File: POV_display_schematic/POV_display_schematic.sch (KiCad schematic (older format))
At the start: 124 parts, among them J1 5-Wire Programming Port, J2 BOOT SELECT, Q1 MMBT3904, Q2 MMBT3906, U1 74HC595, U10 74HC595, U11 HT7325, U2 74HC595, U3 74HC595, U4 74HC595, U5 74HC595, U6 LN4913, U7 74HC595, U8 74HC595, U9 STM32L051C8Tx, Y1 32.768 KHz

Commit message: Uploaded offline work
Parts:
- removed C6: 1uF, Capacitor_SMD:C_1206_3216Metric_Pad1.33x1.80mm_HandSolder, symbol Device:C
- removed J1: 5-Wire Programming Port, Connector_PinHeader_2.54mm:PinHeader_1x05_P2.54mm_Vertical, symbol Connector:Conn_01x05_Female
- removed J2: BOOT SELECT, Connector_PinHeader_2.54mm:PinHeader_1x02_P2.54mm_Vertical, symbol Connector:Conn_01x02_Male
- removed R65: 10K, Resistor_SMD:R_0603_1608Metric_Pad0.98x0.95mm_HandSolder, symbol Device:R
- removed U6: LN4913, Package_TO_SOT_SMD:TSOT-23_HandSoldering, symbol POV_display_schematic:LN4913
- added C2, C4: 10uF, Capacitor_SMD:C_0805_2012Metric_Pad1.18x1.45mm_HandSolder, symbol Device:C
- added D1: Green, LED_SMD:LED_0805_2012Metric_Pad1.15x1.40mm_HandSolder, symbol Device:LED
- added D2: Red, LED_SMD:LED_0805_2012Metric_Pad1.15x1.40mm_HandSolder, symbol Device:LED
- added D24: D_Photo, LED_THT:LED_D5.0mm, symbol Device:D_Photo
- added H1, H2, H3, H4: M3, MountingHole:MountingHole_3.2mm_M3, symbol Mechanical:MountingHole
- added J1: USB_B_Micro, Connector_USB:USB_Micro-B_Molex-105017-0001, symbol Connector:USB_B_Micro
- added J3: HC05/06 Port, Connector_PinHeader_2.54mm:PinHeader_1x04_P2.54mm_Vertical, symbol Connector:Conn_01x04_Female
- added J4: 6PinDebugPort, Connector_IDC:IDC-Header_2x03_P2.54mm_Vertical, symbol MYCLEO:6PinDebugPort
- added R1, R2: 1K, Resistor_SMD:R_0805_2012Metric_Pad1.20x1.40mm_HandSolder, symbol Device:R
- added R10: 10K, Resistor_SMD:R_0805_2012Metric_Pad1.20x1.40mm_HandSolder, symbol Device:R
- added R3, R4: 47K, Resistor_SMD:R_0805_2012Metric_Pad1.20x1.40mm_HandSolder, symbol Device:R
- added R5: 4K7, Resistor_SMD:R_0805_2012Metric_Pad1.20x1.40mm_HandSolder, symbol Device:R
- added SW1: RST, custom_buttons_switches:TSB008, symbol Switch:SW_Push
- added SW2: BOOT, custom_buttons_switches:TSB008, symbol Switch:SW_Push
- added TP1, TP2, TP3, TP4, TP5, TP6: TestPoint, TestPoint:TestPoint_Pad_2.0x2.0mm, symbol Connector:TestPoint
- added U2: TP4056, Package_SO:SOP-8_3.9x4.9mm_P1.27mm, symbol Battery_Management_Custom:TP4056
- C1: renamed from C15; footprint Capacitor_SMD:C_1206_3216Metric_Pad1.33x1.80mm_HandSolder -> Capacitor_SMD:C_0805_2012Metric_Pad1.18x1.45mm_HandSolder
- C10: renamed from C9; footprint Capacitor_SMD:C_1206_3216Metric_Pad1.33x1.80mm_HandSolder -> Capacitor_SMD:C_0805_2012Metric_Pad1.18x1.45mm_HandSolder
- C11: renamed from C5; footprint Capacitor_SMD:C_1206_3216Metric_Pad1.33x1.80mm_HandSolder -> Capacitor_SMD:C_0805_2012Metric_Pad1.18x1.45mm_HandSolder
- C12: renamed from C11; footprint Capacitor_SMD:C_1206_3216Metric_Pad1.33x1.80mm_HandSolder -> Capacitor_SMD:C_0805_2012Metric_Pad1.18x1.45mm_HandSolder
- C13: renamed from C7; footprint Capacitor_SMD:C_1206_3216Metric_Pad1.33x1.80mm_HandSolder -> Capacitor_SMD:C_0805_2012Metric_Pad1.18x1.45mm_HandSolder
- C14: renamed from C10; footprint Capacitor_SMD:C_1206_3216Metric_Pad1.33x1.80mm_HandSolder -> Capacitor_SMD:C_0805_2012Metric_Pad1.18x1.45mm_HandSolder
- C15: renamed from C17; footprint Capacitor_SMD:C_1206_3216Metric_Pad1.33x1.80mm_HandSolder -> Capacitor_SMD:C_0805_2012Metric_Pad1.18x1.45mm_HandSolder
- C16: renamed from C14; footprint Capacitor_SMD:C_1206_3216Metric_Pad1.33x1.80mm_HandSolder -> Capacitor_SMD:C_0805_2012Metric_Pad1.18x1.45mm_HandSolder
- C3: renamed from C16; footprint Capacitor_SMD:C_1206_3216Metric_Pad1.33x1.80mm_HandSolder -> Capacitor_SMD:C_0805_2012Metric_Pad1.18x1.45mm_HandSolder
- C5: renamed from C1; footprint Capacitor_SMD:C_1206_3216Metric_Pad1.33x1.80mm_HandSolder -> Capacitor_SMD:C_0805_2012Metric_Pad1.18x1.45mm_HandSolder
- C6: renamed from C2; footprint Capacitor_SMD:C_1206_3216Metric_Pad1.33x1.80mm_HandSolder -> Capacitor_SMD:C_0805_2012Metric_Pad1.18x1.45mm_HandSolder
- C7: renamed from C3; footprint Capacitor_SMD:C_1206_3216Metric_Pad1.33x1.80mm_HandSolder -> Capacitor_SMD:C_0805_2012Metric_Pad1.18x1.45mm_HandSolder
- C8: footprint Capacitor_SMD:C_1206_3216Metric_Pad1.33x1.80mm_HandSolder -> Capacitor_SMD:C_0805_2012Metric_Pad1.18x1.45mm_HandSolder
- C9: renamed from C4; footprint Capacitor_SMD:C_1206_3216Metric_Pad1.33x1.80mm_HandSolder -> Capacitor_SMD:C_0805_2012Metric_Pad1.18x1.45mm_HandSolder
- R11: renamed from R69; footprint Resistor_SMD:R_1206_3216Metric_Pad1.30x1.75mm_HandSolder -> Resistor_SMD:R_0805_2012Metric_Pad1.20x1.40mm_HandSolder
- R12: renamed from R1; footprint Resistor_SMD:R_0603_1608Metric_Pad0.98x0.95mm_HandSolder -> Resistor_SMD:R_0603_1608Metric
- R13: renamed from R2; footprint Resistor_SMD:R_0603_1608Metric_Pad0.98x0.95mm_HandSolder -> Resistor_SMD:R_0603_1608Metric
- R14: renamed from R3; footprint Resistor_SMD:R_0603_1608Metric_Pad0.98x0.95mm_HandSolder -> Resistor_SMD:R_0603_1608Metric
- R15: renamed from R4; footprint Resistor_SMD:R_0603_1608Metric_Pad0.98x0.95mm_HandSolder -> Resistor_SMD:R_0603_1608Metric
- R16: renamed from R5; footprint Resistor_SMD:R_0603_1608Metric_Pad0.98x0.95mm_HandSolder -> Resistor_SMD:R_0603_1608Metric
- R17: renamed from R6; footprint Resistor_SMD:R_0603_1608Metric_Pad0.98x0.95mm_HandSolder -> Resistor_SMD:R_0603_1608Metric
- R18: renamed from R7; footprint Resistor_SMD:R_0603_1608Metric_Pad0.98x0.95mm_HandSolder -> Resistor_SMD:R_0603_1608Metric
- R19: renamed from R8; footprint Resistor_SMD:R_0603_1608Metric_Pad0.98x0.95mm_HandSolder -> Resistor_SMD:R_0603_1608Metric
- R20: renamed from R9; footprint Resistor_SMD:R_0603_1608Metric_Pad0.98x0.95mm_HandSolder -> Resistor_SMD:R_0603_1608Metric
- R21: renamed from R10; footprint Resistor_SMD:R_0603_1608Metric_Pad0.98x0.95mm_HandSolder -> Resistor_SMD:R_0603_1608Metric
- R22: renamed from R11; footprint Resistor_SMD:R_0603_1608Metric_Pad0.98x0.95mm_HandSolder -> Resistor_SMD:R_0603_1608Metric
- R23: renamed from R12; footprint Resistor_SMD:R_0603_1608Metric_Pad0.98x0.95mm_HandSolder -> Resistor_SMD:R_0603_1608Metric
- R24: renamed from R13; footprint Resistor_SMD:R_0603_1608Metric_Pad0.98x0.95mm_HandSolder -> Resistor_SMD:R_0603_1608Metric
- R25: renamed from R14; footprint Resistor_SMD:R_0603_1608Metric_Pad0.98x0.95mm_HandSolder -> Resistor_SMD:R_0603_1608Metric
- R26: renamed from R15; footprint Resistor_SMD:R_0603_1608Metric_Pad0.98x0.95mm_HandSolder -> Resistor_SMD:R_0603_1608Metric
- R27: renamed from R16; footprint Resistor_SMD:R_0603_1608Metric_Pad0.98x0.95mm_HandSolder -> Resistor_SMD:R_0603_1608Metric
- R28: renamed from R17; footprint Resistor_SMD:R_0603_1608Metric_Pad0.98x0.95mm_HandSolder -> Resistor_SMD:R_0603_1608Metric
- R29: renamed from R18; footprint Resistor_SMD:R_0603_1608Metric_Pad0.98x0.95mm_HandSolder -> Resistor_SMD:R_0603_1608Metric
- R30: renamed from R19; footprint Resistor_SMD:R_0603_1608Metric_Pad0.98x0.95mm_HandSolder -> Resistor_SMD:R_0603_1608Metric
- R31: renamed from R20; footprint Resistor_SMD:R_0603_1608Metric_Pad0.98x0.95mm_HandSolder -> Resistor_SMD:R_0603_1608Metric
- R32: renamed from R21; footprint Resistor_SMD:R_0603_1608Metric_Pad0.98x0.95mm_HandSolder -> Resistor_SMD:R_0603_1608Metric
- R33: renamed from R22; footprint Resistor_SMD:R_0603_1608Metric_Pad0.98x0.95mm_HandSolder -> Resistor_SMD:R_0603_1608Metric
- R34: renamed from R23; footprint Resistor_SMD:R_0603_1608Metric_Pad0.98x0.95mm_HandSolder -> Resistor_SMD:R_0603_1608Metric
- R35: renamed from R24; footprint Resistor_SMD:R_0603_1608Metric_Pad0.98x0.95mm_HandSolder -> Resistor_SMD:R_0603_1608Metric
- R36: renamed from R25; footprint Resistor_SMD:R_0603_1608Metric_Pad0.98x0.95mm_HandSolder -> Resistor_SMD:R_0603_1608Metric
- R37: renamed from R26; footprint Resistor_SMD:R_0603_1608Metric_Pad0.98x0.95mm_HandSolder -> Resistor_SMD:R_0603_1608Metric
- R38: renamed from R27; footprint Resistor_SMD:R_0603_1608Metric_Pad0.98x0.95mm_HandSolder -> Resistor_SMD:R_0603_1608Metric
- R39: renamed from R28; footprint Resistor_SMD:R_0603_1608Metric_Pad0.98x0.95mm_HandSolder -> Resistor_SMD:R_0603_1608Metric
- R40: renamed from R29; footprint Resistor_SMD:R_0603_1608Metric_Pad0.98x0.95mm_HandSolder -> Resistor_SMD:R_0603_1608Metric
- R41: renamed from R30; footprint Resistor_SMD:R_0603_1608Metric_Pad0.98x0.95mm_HandSolder -> Resistor_SMD:R_0603_1608Metric
- R42: renamed from R31; footprint Resistor_SMD:R_0603_1608Metric_Pad0.98x0.95mm_HandSolder -> Resistor_SMD:R_0603_1608Metric
- R43: renamed from R32; footprint Resistor_SMD:R_0603_1608Metric_Pad0.98x0.95mm_HandSolder -> Resistor_SMD:R_0603_1608Metric
- R44: renamed from R33; footprint Resistor_SMD:R_0603_1608Metric_Pad0.98x0.95mm_HandSolder -> Resistor_SMD:R_0603_1608Metric
- R45: renamed from R34; footprint Resistor_SMD:R_0603_1608Metric_Pad0.98x0.95mm_HandSolder -> Resistor_SMD:R_0603_1608Metric
- R46: renamed from R35; footprint Resistor_SMD:R_0603_1608Metric_Pad0.98x0.95mm_HandSolder -> Resistor_SMD:R_0603_1608Metric
- R47: renamed from R36; footprint Resistor_SMD:R_0603_1608Metric_Pad0.98x0.95mm_HandSolder -> Resistor_SMD:R_0603_1608Metric
- R48: renamed from R37; footprint Resistor_SMD:R_0603_1608Metric_Pad0.98x0.95mm_HandSolder -> Resistor_SMD:R_0603_1608Metric
- R49: renamed from R38; footprint Resistor_SMD:R_0603_1608Metric_Pad0.98x0.95mm_HandSolder -> Resistor_SMD:R_0603_1608Metric
- R50: renamed from R39; footprint Resistor_SMD:R_0603_1608Metric_Pad0.98x0.95mm_HandSolder -> Resistor_SMD:R_0603_1608Metric
- R51: renamed from R40; footprint Resistor_SMD:R_0603_1608Metric_Pad0.98x0.95mm_HandSolder -> Resistor_SMD:R_0603_1608Metric
- R52: renamed from R41; footprint Resistor_SMD:R_0603_1608Metric_Pad0.98x0.95mm_HandSolder -> Resistor_SMD:R_0603_1608Metric
- R53: renamed from R42; footprint Resistor_SMD:R_0603_1608Metric_Pad0.98x0.95mm_HandSolder -> Resistor_SMD:R_0603_1608Metric
- R54: renamed from R43; footprint Resistor_SMD:R_0603_1608Metric_Pad0.98x0.95mm_HandSolder -> Resistor_SMD:R_0603_1608Metric
- R55: renamed from R44; footprint Resistor_SMD:R_0603_1608Metric_Pad0.98x0.95mm_HandSolder -> Resistor_SMD:R_0603_1608Metric
- R56: renamed from R45; footprint Resistor_SMD:R_0603_1608Metric_Pad0.98x0.95mm_HandSolder -> Resistor_SMD:R_0603_1608Metric
- R57: renamed from R46; footprint Resistor_SMD:R_0603_1608Metric_Pad0.98x0.95mm_HandSolder -> Resistor_SMD:R_0603_1608Metric
- R58: renamed from R47; footprint Resistor_SMD:R_0603_1608Metric_Pad0.98x0.95mm_HandSolder -> Resistor_SMD:R_0603_1608Metric
- R59: renamed from R48; footprint Resistor_SMD:R_0603_1608Metric_Pad0.98x0.95mm_HandSolder -> Resistor_SMD:R_0603_1608Metric
- R6: renamed from R66; footprint Resistor_SMD:R_1206_3216Metric_Pad1.30x1.75mm_HandSolder -> Resistor_SMD:R_0805_2012Metric_Pad1.20x1.40mm_HandSolder
- R60: renamed from R49; footprint Resistor_SMD:R_0603_1608Metric_Pad0.98x0.95mm_HandSolder -> Resistor_SMD:R_0603_1608Metric
- R61: renamed from R50; footprint Resistor_SMD:R_0603_1608Metric_Pad0.98x0.95mm_HandSolder -> Resistor_SMD:R_0603_1608Metric
- R62: renamed from R51; footprint Resistor_SMD:R_0603_1608Metric_Pad0.98x0.95mm_HandSolder -> Resistor_SMD:R_0603_1608Metric
- R63: renamed from R52; footprint Resistor_SMD:R_0603_1608Metric_Pad0.98x0.95mm_HandSolder -> Resistor_SMD:R_0603_1608Metric
- R64: renamed from R53; footprint Resistor_SMD:R_0603_1608Metric_Pad0.98x0.95mm_HandSolder -> Resistor_SMD:R_0603_1608Metric
- R65: renamed from R54; footprint Resistor_SMD:R_0603_1608Metric_Pad0.98x0.95mm_HandSolder -> Resistor_SMD:R_0603_1608Metric
- R66: renamed from R55; footprint Resistor_SMD:R_0603_1608Metric_Pad0.98x0.95mm_HandSolder -> Resistor_SMD:R_0603_1608Metric
- R67: renamed from R56; footprint Resistor_SMD:R_0603_1608Metric_Pad0.98x0.95mm_HandSolder -> Resistor_SMD:R_0603_1608Metric
- R68: renamed from R57; footprint Resistor_SMD:R_0603_1608Metric_Pad0.98x0.95mm_HandSolder -> Resistor_SMD:R_0603_1608Metric
- R69: renamed from R58; footprint Resistor_SMD:R_0603_1608Metric_Pad0.98x0.95mm_HandSolder -> Resistor_SMD:R_0603_1608Metric
- R7: renamed from R64; footprint Resistor_SMD:R_0603_1608Metric_Pad0.98x0.95mm_HandSolder -> Resistor_SMD:R_0805_2012Metric_Pad1.20x1.40mm_HandSolder
- R70: renamed from R59; footprint Resistor_SMD:R_0603_1608Metric_Pad0.98x0.95mm_HandSolder -> Resistor_SMD:R_0603_1608Metric
- R71: renamed from R60; footprint Resistor_SMD:R_0603_1608Metric_Pad0.98x0.95mm_HandSolder -> Resistor_SMD:R_0603_1608Metric
- R72: renamed from R61; footprint Resistor_SMD:R_0603_1608Metric_Pad0.98x0.95mm_HandSolder -> Resistor_SMD:R_0603_1608Metric
- R73: renamed from R62; footprint Resistor_SMD:R_0603_1608Metric_Pad0.98x0.95mm_HandSolder -> Resistor_SMD:R_0603_1608Metric
- R74: renamed from R63; footprint Resistor_SMD:R_0603_1608Metric_Pad0.98x0.95mm_HandSolder -> Resistor_SMD:R_0603_1608Metric
- R8: renamed from R67; footprint Resistor_SMD:R_1206_3216Metric_Pad1.30x1.75mm_HandSolder -> Resistor_SMD:R_0805_2012Metric_Pad1.20x1.40mm_HandSolder
- R9: renamed from R68; footprint Resistor_SMD:R_1206_3216Metric_Pad1.30x1.75mm_HandSolder -> Resistor_SMD:R_0805_2012Metric_Pad1.20x1.40mm_HandSolder
- renumbered C12 to C17, C13 to C18, D8 to D10, D9 to D11, D10 to D12, D11 to D13, D12 to D14, D13 to D15, D14 to D16, D15 to D17, D16 to D18, D17 to D19, D18 to D20, D19 to D21, D20 to D22, D21 to D23, D1 to D3, D2 to D4, D3 to D5, D4 to D6, D5 to D7, D6 to D8, D7 to D9, Q1 to Q2, Q2 to Q3, U11 to U1, U4 to U10, U10 to U11, U5 to U3, U1 to U4, U2 to U5, U7 to U6, U3 to U7
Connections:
- net +BATT: now also C4.1, TP6.1, U2.5 (Bat)
- net BAT_EN: now also U9.12 (PA2); no longer U9.46 (PB9)
- net BAT_IN: now also U9.13 (PA3), TP4.1; no longer U9.10 (PA0)
- net GND: now also C2.2, C4.2, D24.2 (A), J1.4 (ID), J1.5 (GND), J1.6 (Shield), J3.2 (Pin_2), J4.1 (Gnd), R4.2, R5.2, SW1.2, TP2.1, U2.1 (Temp), U2.3 (Gnd)
- net SWCLK: now also J4.2 (SWCLK)
- net SWDIO: now also J4.3 (SWDIO)
- net VCC: now also J3.1 (Pin_1), J4.6 (VCC), R10.1, SW2.1, TP1.1
- net boot: now also SW2.2
- net ~rst: now also J4.4 (RST), R10.2, SW1.1
- net FDBK: now reaches U9.2 (PC13)
- net FDBK: now also R7.2, D24.1 (K), TP3.1
- net MCU_TX: now reaches U9.30 (PA9)
- net MCU_TX: now also J3.4 (Pin_4)
- net MCU_RX: now reaches U9.31 (PA10)
- net MCU_RX: now also J3.3 (Pin_3)
- net hall_sig: no longer names the net of U9.41 (PB5)
- net hall_sig: no longer R7.2
- new net: R5.1, U2.2 (Prog)
- new net: R2.2, U2.6 (~STDBY)
- new net: R1.1, U2.7 (~CHRG)
- new net: D2.1 (K), R2.1
- new net: D1.1 (K), R1.2
- new net +5V: C2.1, D1.2 (A), D2.2 (A), J1.1 (VBUS), R3.1, TP5.1, U2.4 (Vcc), U2.8 (CE)
- new net USB_Flag: R3.2, R4.1, U9.46 (PB9)
- no-connect marks 0 -> 2
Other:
- note added: "Battery Charger"
- note added: "Battery Mounting Holes"
- note added: "Battery Voltage \nMeasuring Circuit"
- note added: "Battery size:\n50x34x6mm"
- note added: "Bluetooth\nSerial Port"
- note added: "Boot/ Rst\nSwitches"
- note added: "Feedback"
- note added: "SIPO Registers' \nDecoupling Capacitors"
- note added: "Testing Points"
- note added: "USB Charging Port"
- note added: "Voltage Regulator 3V3"
- note removed: "Battery Voltage Measuring Circuit"
- note removed: "Boot Jumper"
- note removed: "Hall Sensor"
- note removed: "SIPO Registers' Decoupling Capacitors"
- note removed: "Voltage Regulator 2.5V"
- moved on the sheet: C10, C11, C12, C13, C14, C15, C16, C17, C18, C5, C6, C7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

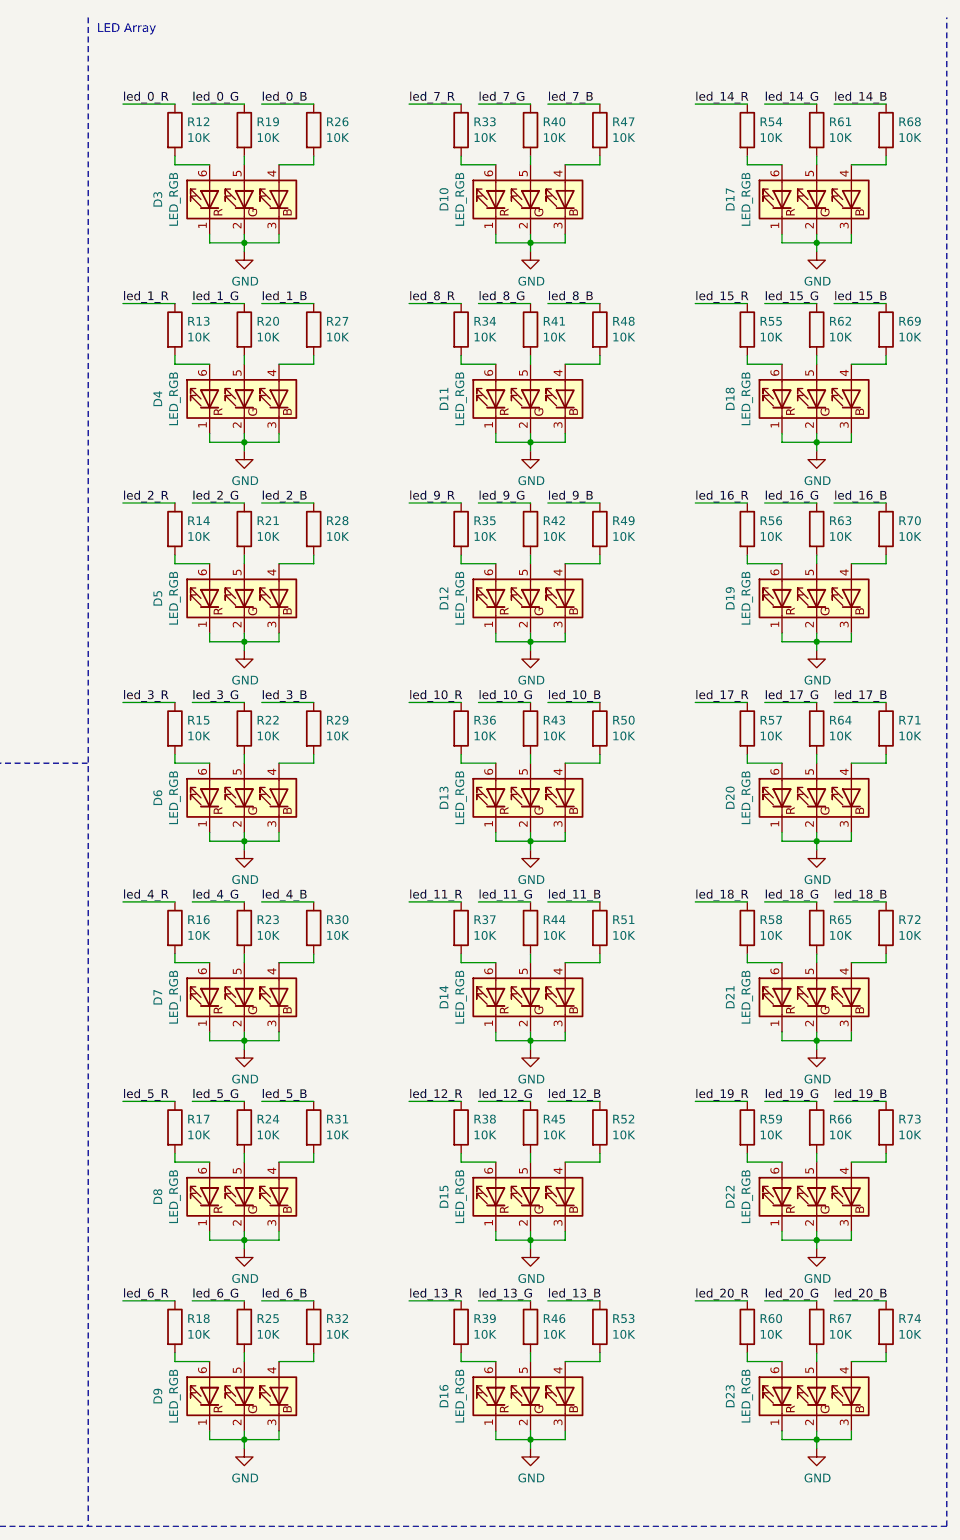
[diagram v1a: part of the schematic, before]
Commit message: LEDs footprints are now in correct orientation
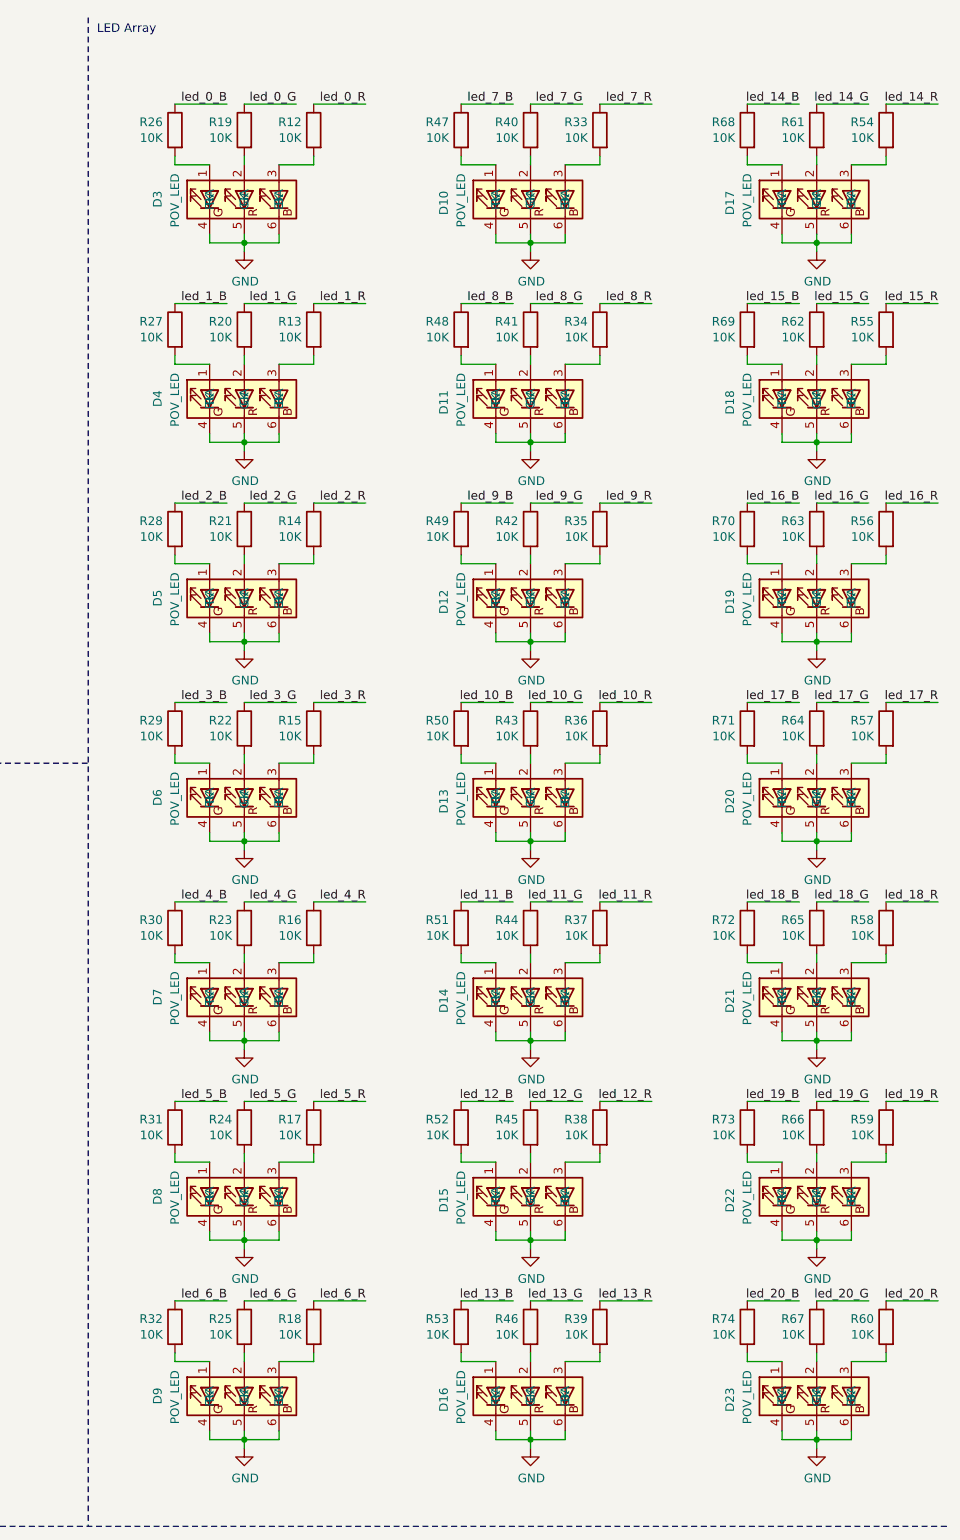
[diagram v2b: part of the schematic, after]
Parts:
- removed D10, D11, D12, D13, D14, D15, D16, D17, D18, D19, D20, D21, D22, D23, D3, D4, D5, D6, D7, D8, D9: LED_RGB, LED_SMD:LED_RGB_5050-6, symbol Device:LED_RGB
- added D10, D11, D12, D13, D14, D15, D16, D17, D18, D19, D20, D21, D22, D23, D3, D4, D5, D6, D7, D8, D9: POV_LED, LED_SMD:LED_RGB_5050-6, symbol POV_display_schematic:POV_LED
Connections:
- net GND: now also D10.4 (RK), D10.5 (GK), D10.6 (BK), D11.4 (RK), D11.5 (GK), D11.6 (BK), D12.4 (RK), D12.5 (GK), D12.6 (BK), D13.4 (RK), D13.5 (GK), D13.6 (BK), D14.4 (RK), D14.5 (GK), D14.6 (BK), D15.4 (RK), D15.5 (GK), D15.6 (BK), D16.4 (RK), D16.5 (GK), D16.6 (BK), D17.4 (RK), D17.5 (GK), D17.6 (BK), D18.4 (RK), D18.5 (GK), D18.6 (BK), D19.4 (RK), D19.5 (GK), D19.6 (BK), D20.4 (RK), D20.5 (GK), D20.6 (BK), D21.4 (RK), D21.5 (GK), D21.6 (BK), D22.4 (RK), D22.5 (GK), D22.6 (BK), D23.4 (RK), D23.5 (GK), D23.6 (BK), D3.4 (RK), D3.5 (GK), D3.6 (BK), D4.4 (RK), D4.5 (GK), D4.6 (BK), D5.4 (RK), D5.5 (GK), D5.6 (BK), D6.4 (RK), D6.5 (GK), D6.6 (BK), D7.4 (RK), D7.5 (GK), D7.6 (BK), D8.4 (RK), D8.5 (GK), D8.6 (BK), D9.4 (RK), D9.5 (GK), D9.6 (BK)
- net at R19.2: now also D3.2 (GA)
- net at R26.2: now also D3.1 (RA)
- net at R12.2: now also D3.3 (BA)
- net at R13.2: now also D4.3 (BA)
- net at R20.2: now also D4.2 (GA)
- net at R27.2: now also D4.1 (RA)
- net at R14.2: now also D5.3 (BA)
- net at R21.2: now also D5.2 (GA)
- net at R28.2: now also D5.1 (RA)
- net at R15.2: now also D6.3 (BA)
- net at R22.2: now also D6.2 (GA)
- net at R29.2: now also D6.1 (RA)
- net at R16.2: now also D7.3 (BA)
- net at R23.2: now also D7.2 (GA)
- net at R30.2: now also D7.1 (RA)
- net at R17.2: now also D8.3 (BA)
- net at R24.2: now also D8.2 (GA)
- net at R31.2: now also D8.1 (RA)
- net at R18.2: now also D9.3 (BA)
- net at R25.2: now also D9.2 (GA)
- net at R32.2: now also D9.1 (RA)
- net at R33.2: now also D10.3 (BA)
- net at R40.2: now also D10.2 (GA)
- net at R47.2: now also D10.1 (RA)
- net at R34.2: now also D11.3 (BA)
- net at R41.2: now also D11.2 (GA)
- net at R48.2: now also D11.1 (RA)
- net at R35.2: now also D12.3 (BA)
- net at R42.2: now also D12.2 (GA)
- net at R49.2: now also D12.1 (RA)
- net at R36.2: now also D13.3 (BA)
- net at R43.2: now also D13.2 (GA)
- net at R50.2: now also D13.1 (RA)
- net at R37.2: now also D14.3 (BA)
- net at R44.2: now also D14.2 (GA)
- net at R51.2: now also D14.1 (RA)
- net at R38.2: now also D15.3 (BA)
- net at R45.2: now also D15.2 (GA)
- net at R52.2: now also D15.1 (RA)
- net at R39.2: now also D16.3 (BA)
- net at R46.2: now also D16.2 (GA)
- net at R53.2: now also D16.1 (RA)
- net at R54.2: now also D17.3 (BA)
- net at R61.2: now also D17.2 (GA)
- net at R68.2: now also D17.1 (RA)
- net at R55.2: now also D18.3 (BA)
- net at R62.2: now also D18.2 (GA)
- net at R69.2: now also D18.1 (RA)
- net at R56.2: now also D19.3 (BA)
- net at R63.2: now also D19.2 (GA)
- net at R70.2: now also D19.1 (RA)
- net at R57.2: now also D20.3 (BA)
- net at R64.2: now also D20.2 (GA)
- net at R71.2: now also D20.1 (RA)
- net at R58.2: now also D21.3 (BA)
- net at R65.2: now also D21.2 (GA)
- net at R72.2: now also D21.1 (RA)
- net at R59.2: now also D22.3 (BA)
- net at R66.2: now also D22.2 (GA)
- net at R73.2: now also D22.1 (RA)
- net at R60.2: now also D23.3 (BA)
- net at R67.2: now also D23.2 (GA)
- net at R74.2: now also D23.1 (RA)
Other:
- moved on the sheet: R12, R13, R14, R15, R16, R17, R18, R26, R27, R28, R29, R30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
